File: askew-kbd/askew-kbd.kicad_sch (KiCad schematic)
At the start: 57 parts, among them J1 OLED, J2 MJ-4PP-9, SW1 SW_PUSH, SW10 SW_PUSH, SW11 SW_PUSH, SW12 SW_PUSH, SW13 SW_PUSH, SW14 SW_PUSH, SW15 SW_PUSH, SW16 SW_PUSH, SW17 SW_PUSH, SW18 SW_PUSH, SW19 SW_PUSH, SW2 SW_PUSH, SW20 SW_PUSH, SW21 SW_PUSH, SW22 SW_PUSH, SW3 SW_PUSH, SW4 SW_PUSH, SW5 SW_PUSH, SW6 SW_PUSH, SW7 SW_PUSH, SW8 SW_PUSH, SW9 SW_PUSH, U1 ProMicro

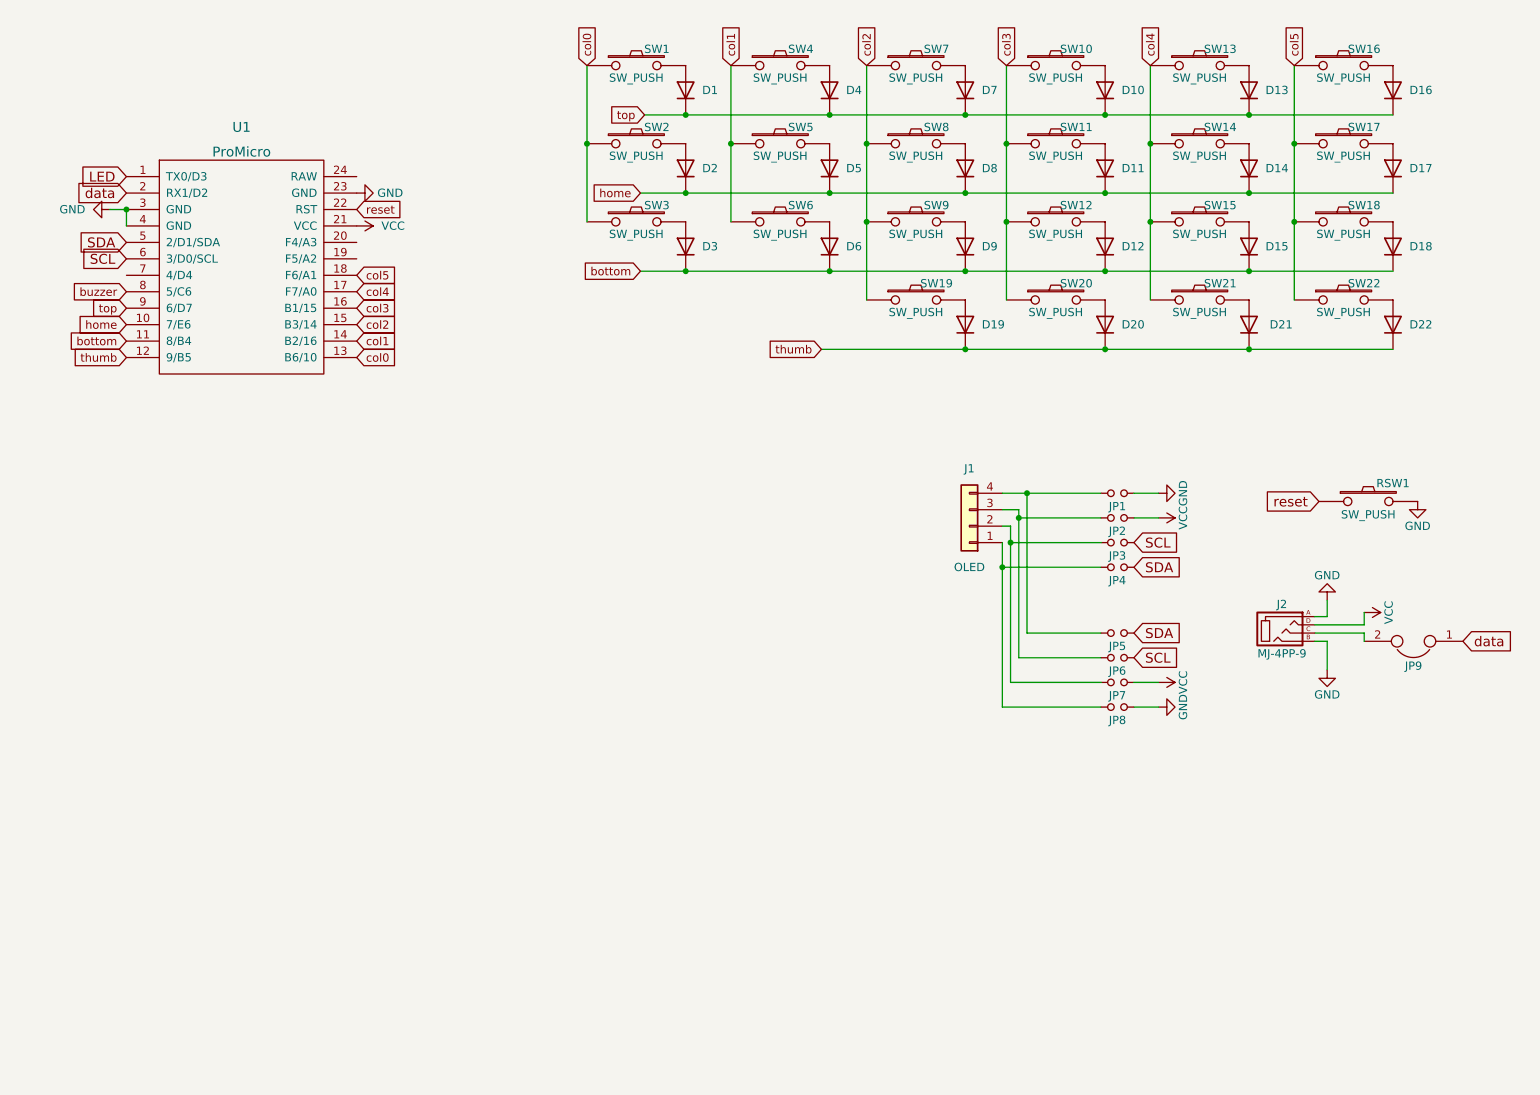
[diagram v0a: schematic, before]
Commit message: add rotary
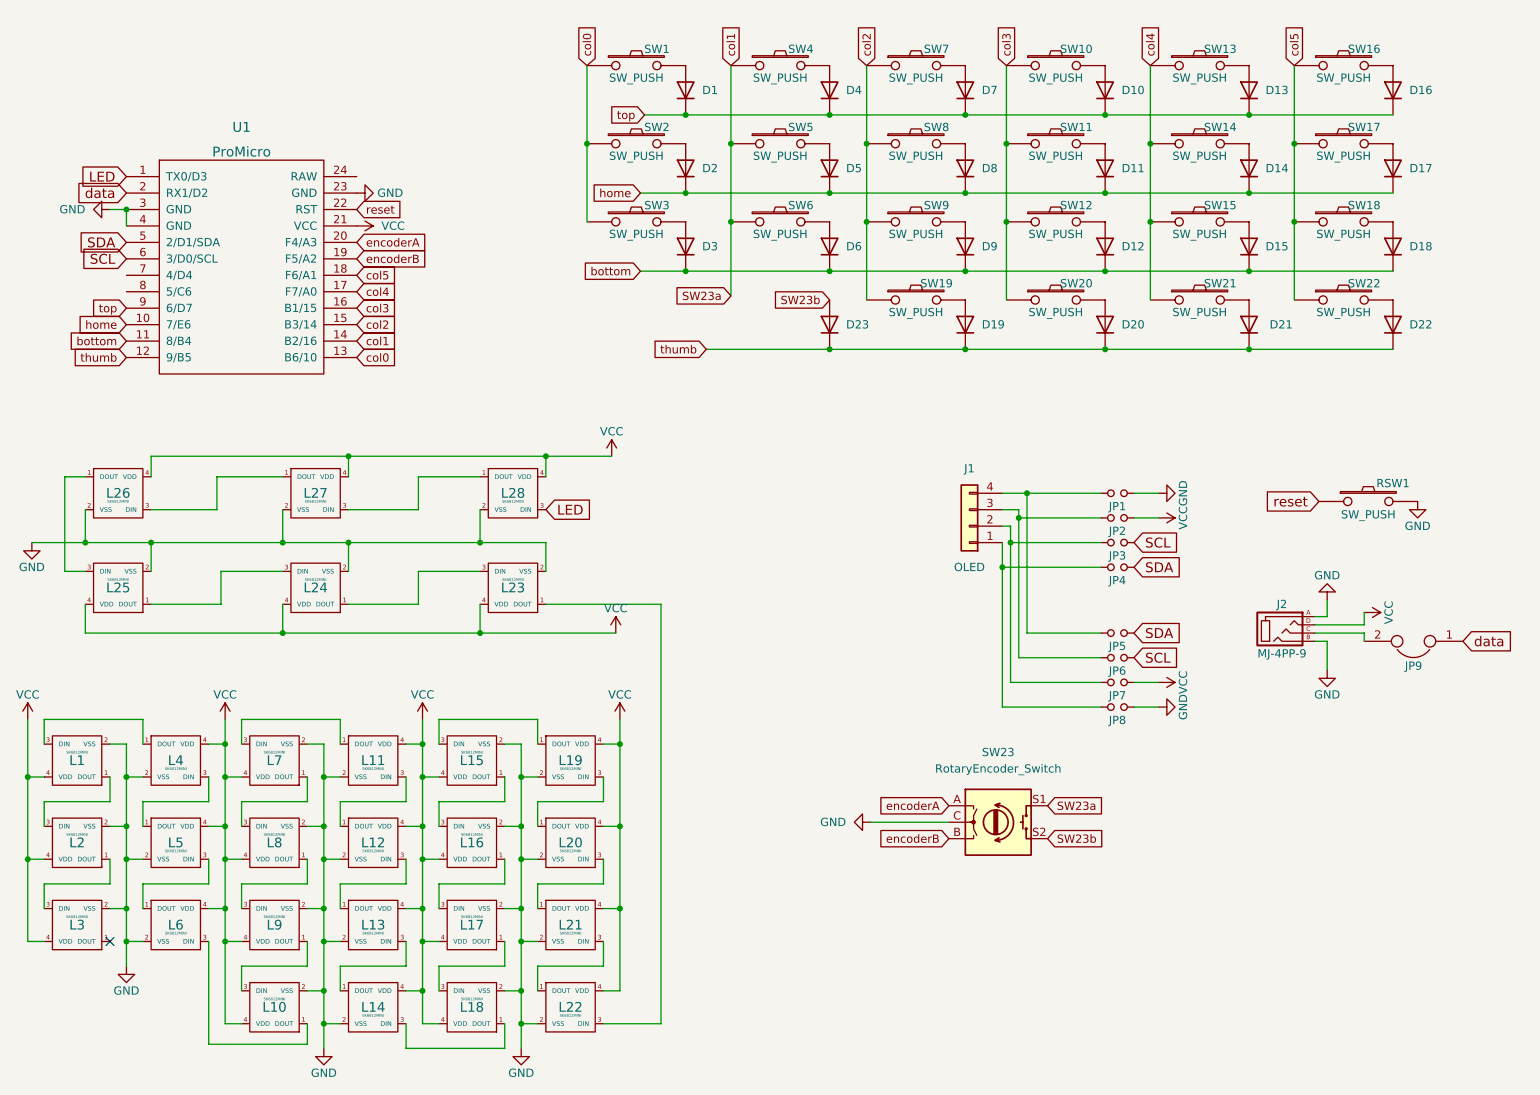
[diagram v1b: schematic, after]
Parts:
- added D23: DIODE, fp:D3_SMD, symbol Simulation_SPICE:DIODE
- added L1, L10, L11, L12, L13, L14, L15, L16, L17, L18, L19, L2, L20, L21, L22, L3, L4, L5, L6, L7, L8, L9: SK6812MINI, fp:SK6812MINI_rev, symbol corne-chocolate-rescue:SK6812MINI-kbd
- added L23, L24, L25, L26, L27, L28: SK6812MINI, fp:SK6812MINI_underglow_rev, symbol corne-chocolate-rescue:SK6812MINI-kbd
- added SW23: RotaryEncoder_Switch, Rotary_Encoder:RotaryEncoder_Alps_EC11E-Switch_Vertical_H20mm, symbol Device:RotaryEncoder_Switch
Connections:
- net GND: now also L1.2 (VSS), L10.2 (VSS), L11.2 (VSS), L12.2 (VSS), L13.2 (VSS), L14.2 (VSS), L15.2 (VSS), L16.2 (VSS), L17.2 (VSS), L18.2 (VSS), L19.2 (VSS), L2.2 (VSS), L20.2 (VSS), L21.2 (VSS), L22.2 (VSS), L23.2 (VSS), L24.2 (VSS), L25.2 (VSS), L26.2 (VSS), L27.2 (VSS), L28.2 (VSS), L3.2 (VSS), L4.2 (VSS), L5.2 (VSS), L6.2 (VSS), L7.2 (VSS), L8.2 (VSS), L9.2 (VSS), SW23.C
- net LED: now also L28.3 (DIN)
- net VCC: now also L1.4 (VDD), L10.4 (VDD), L11.4 (VDD), L12.4 (VDD), L13.4 (VDD), L14.4 (VDD), L15.4 (VDD), L16.4 (VDD), L17.4 (VDD), L18.4 (VDD), L19.4 (VDD), L2.4 (VDD), L20.4 (VDD), L21.4 (VDD), L22.4 (VDD), L23.4 (VDD), L24.4 (VDD), L25.4 (VDD), L26.4 (VDD), L27.4 (VDD), L28.4 (VDD), L3.4 (VDD), L4.4 (VDD), L5.4 (VDD), L6.4 (VDD), L7.4 (VDD), L8.4 (VDD), L9.4 (VDD)
- net thumb: now also D23.2 (K)
- net encoderB: now reaches U1.19 (F5/A2)
- net encoderB: now also SW23.B
- net encoderA: now reaches U1.20 (F4/A3)
- net encoderA: now also SW23.A
- net buzzer: no longer names the net of U1.8 (5/C6)
- net col1 renamed SW23a
- net SW23a: now also SW23.S1
- new net: L21.3 (DIN), L22.1 (DOUT)
- new net: L22.3 (DIN), L23.1 (DOUT)
- new net: L23.3 (DIN), L24.1 (DOUT)
- new net: L24.3 (DIN), L25.1 (DOUT)
- new net: L15.3 (DIN), L19.1 (DOUT)
- new net: L19.3 (DIN), L20.1 (DOUT)
- new net: L4.3 (DIN), L5.1 (DOUT)
- new net: L5.3 (DIN), L6.1 (DOUT)
- new net: L10.1 (DOUT), L6.3 (DIN)
- new net: L10.3 (DIN), L9.1 (DOUT)
- new net: L8.1 (DOUT), L9.3 (DIN)
- new net: L2.1 (DOUT), L3.3 (DIN)
- new net: L1.1 (DOUT), L2.3 (DIN)
- new net: L7.1 (DOUT), L8.3 (DIN)
- new net: L12.3 (DIN), L13.1 (DOUT)
- new net: L13.3 (DIN), L14.1 (DOUT)
- new net: L17.1 (DOUT), L18.3 (DIN)
- new net: L16.1 (DOUT), L17.3 (DIN)
- new net: L14.3 (DIN), L18.1 (DOUT)
- new net: L11.1 (DOUT), L7.3 (DIN)
- new net: L15.1 (DOUT), L16.3 (DIN)
- new net: L1.3 (DIN), L4.1 (DOUT)
- new net: L27.3 (DIN), L28.1 (DOUT)
- new net: L20.3 (DIN), L21.1 (DOUT)
- new net: L11.3 (DIN), L12.1 (DOUT)
- new net: L25.3 (DIN), L26.1 (DOUT)
- new net: L26.3 (DIN), L27.1 (DOUT)
- new net SW23b: D23.1 (A), SW23.S2
- no-connect marks 0 -> 1

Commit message: promicro routing
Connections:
- no-connect marks 1 -> 4
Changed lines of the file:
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@@
   (junction (at 55.88 160.02) (diameter 0) (color 0 0 0 0)
   )
+  (junction (at 149.225 53.975) (diameter 0) (color 0 0 0 0)
+  )
   (junction (at 71.12 160.02) (diameter 0) (color 0 0 0 0)
   )
@@
   (junction (at 80.01 117.475) (diameter 0) (color 0 0 0 0)
   )
-  (junction (at 149.225 53.975) (diameter 0) (color 0 0 0 0)
-  )
   (junction (at 55.88 147.32) (diameter 0) (color 0 0 0 0)
   )
@@
   )
   (no_connect (at 53.34 165.1))
+  (no_connect (at 55.88 64.77))
+  (no_connect (at 55.88 62.23))
+  (no_connect (at 91.44 46.99))
   (wire (pts (xy 71.12 160.02) (xy 71.12 165.1))
     (stroke (width 0) (type default) (color 0 0 0 0))
@@
     (stroke (width 0) (type default) (color 0 0 0 0))
   )
+  (wire (pts (xy 149.225 53.975) (xy 149.225 66.04))
+    (stroke (width 0) (type default) (color 0 0 0 0))
+  )
   (wire (pts (xy 119.38 172.72) (xy 119.38 168.91))
     (stroke (width 0) (type default) (color 0 0 0 0))
@@
     (stroke (width 0) (type default) (color 0 0 0 0))
   )
-  (wire (pts (xy 149.225 53.975) (xy 149.225 65.405))
-    (stroke (width 0) (type default) (color 0 0 0 0))
-  )
   (wire (pts (xy 229.235 73.66) (xy 251.46 73.66))
     (stroke (width 0) (type default) (color 0 0 0 0))
@@
     (stroke (width 0) (type default) (color 0 0 0 0))
   )
+  (wire (pts (xy 161.29 66.04) (xy 161.29 69.85))
+    (stroke (width 0) (type default) (color 0 0 0 0))
+  )
   (wire (pts (xy 49.53 113.03) (xy 49.53 117.475))
     (stroke (width 0) (type default) (color 0 0 0 0))
@@
     (stroke (width 0) (type default) (color 0 0 0 0))
   )
+  (wire (pts (xy 164.465 66.04) (xy 161.29 66.04))
+    (stroke (width 0) (type default) (color 0 0 0 0))
+  )
   (wire (pts (xy 71.12 165.1) (xy 73.66 165.1))
     (stroke (width 0) (type default) (color 0 0 0 0))
@@
   )
   (wire (pts (xy 71.12 134.62) (xy 71.12 139.7))
+    (stroke (width 0) (type default) (color 0 0 0 0))
+  )
+  (wire (pts (xy 150.495 66.04) (xy 149.225 66.04))
     (stroke (width 0) (type default) (color 0 0 0 0))
   )
@@
     )
   )
-  (global_label "SW23a" (shape input) (at 149.225 65.405 180) (fields_autoplaced)
-    (effects (font (size 1.27 1.27)) (justify right))
-    (property "Intersheet References" "${INTERSHEET_REFS}" (id 0) (at 140.5829 65.3256 0)
-      (effects (font (size 1.27 1.27)) (justify right) hide)
+  (global_label "SW23a" (shape input) (at 150.495 66.04 0) (fields_autoplaced)
+    (effects (font (size 1.27 1.27)) (justify left))
+    (property "Intersheet References" "${INTERSHEET_REFS}" (id 0) (at 159.1371 66.1194 0)
+      (effects (font (size 1.27 1.27)) (justify left) hide)
     )
   )
@@
     )
   )
-  (global_label "SW23b" (shape input) (at 164.465 66.04 180) (fields_autoplaced)
+  (global_label "SW23b" (shape input) (at 161.29 69.85 180) (fields_autoplaced)
     (effects (font (size 1.27 1.27)) (justify right))
-    (property "Intersheet References" "${INTERSHEET_REFS}" (id 0) (at 155.8229 65.9606 0)
+    (property "Intersheet References" "${INTERSHEET_REFS}" (id 0) (at 152.6479 69.7706 0)
       (effects (font (size 1.27 1.27)) (justify right) hide)
     )
